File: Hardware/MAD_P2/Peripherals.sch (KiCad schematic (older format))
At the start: 100 parts, among them J12 Micro_SD_Card, U28 DS3231M, U29 ESP-12F

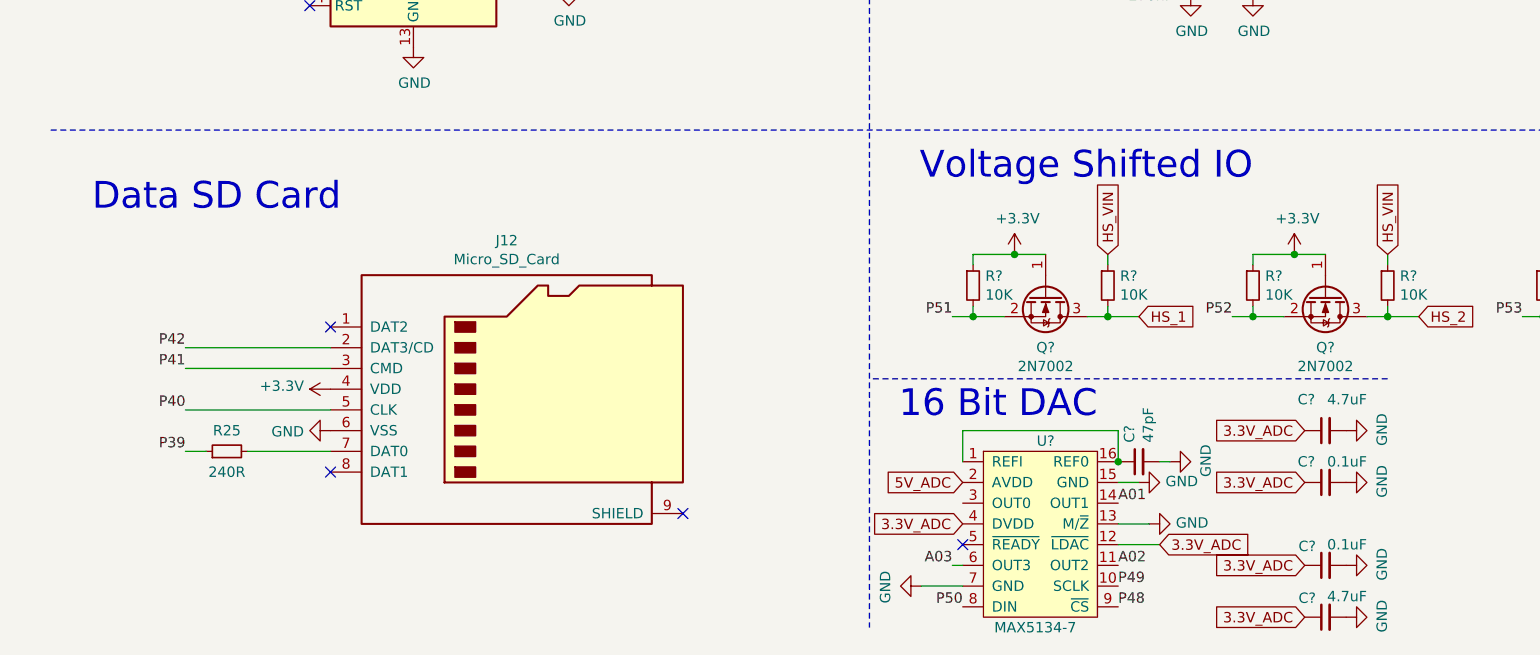
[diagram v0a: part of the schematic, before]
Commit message: added optional sd card socket for data
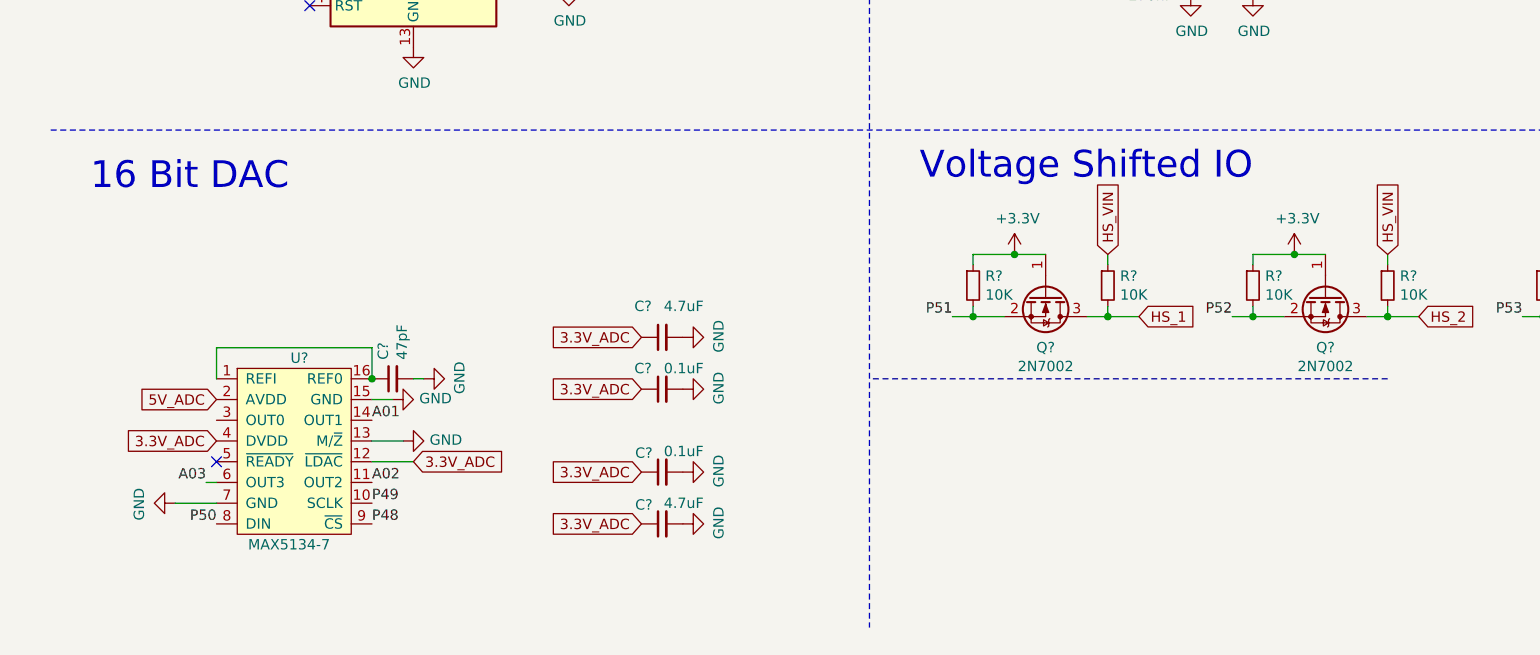
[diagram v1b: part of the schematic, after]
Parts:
- removed J12: Micro_SD_Card, Tensile_Board:WM26501, symbol Connector:Micro_SD_Card
- removed R25: 240R, Resistor_SMD:R_0603_1608Metric, symbol Device:R_Small
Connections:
- no-connect marks 9 -> 6
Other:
- note removed: "Data SD Card"
- moved on the sheet: C?, U?

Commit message: revising pcb layout
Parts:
- C108, C113, C114: renamed from C?; footprint (none) -> Capacitor_SMD:C_0603_1608Metric
- J33: renamed from J?; footprint (none) -> Connector_PinSocket_2.54mm:PinSocket_1x06_P2.54mm_Vertical
- R38, R41, R43, R44, R45, R48, R49, R50, R61: renamed from R?; footprint (none) -> Resistor_SMD:R_0603_1608Metric
- R57, R58, R59, R60, R62, R63, R64, R65: renamed from R?; footprint (none) -> Resistor_SMD:R_0805_2012Metric
- U23: renamed from U?; footprint (none) -> Package_QFP:LQFP-32_5x5mm_P0.5mm
- Y2: renamed from Y?; value Crystal_GND24_Small -> 16.384MHz; footprint (none) -> Crystal:Crystal_SMD_3225-4Pin_3.2x2.5mm
- gave numbers to parts that had none: 47

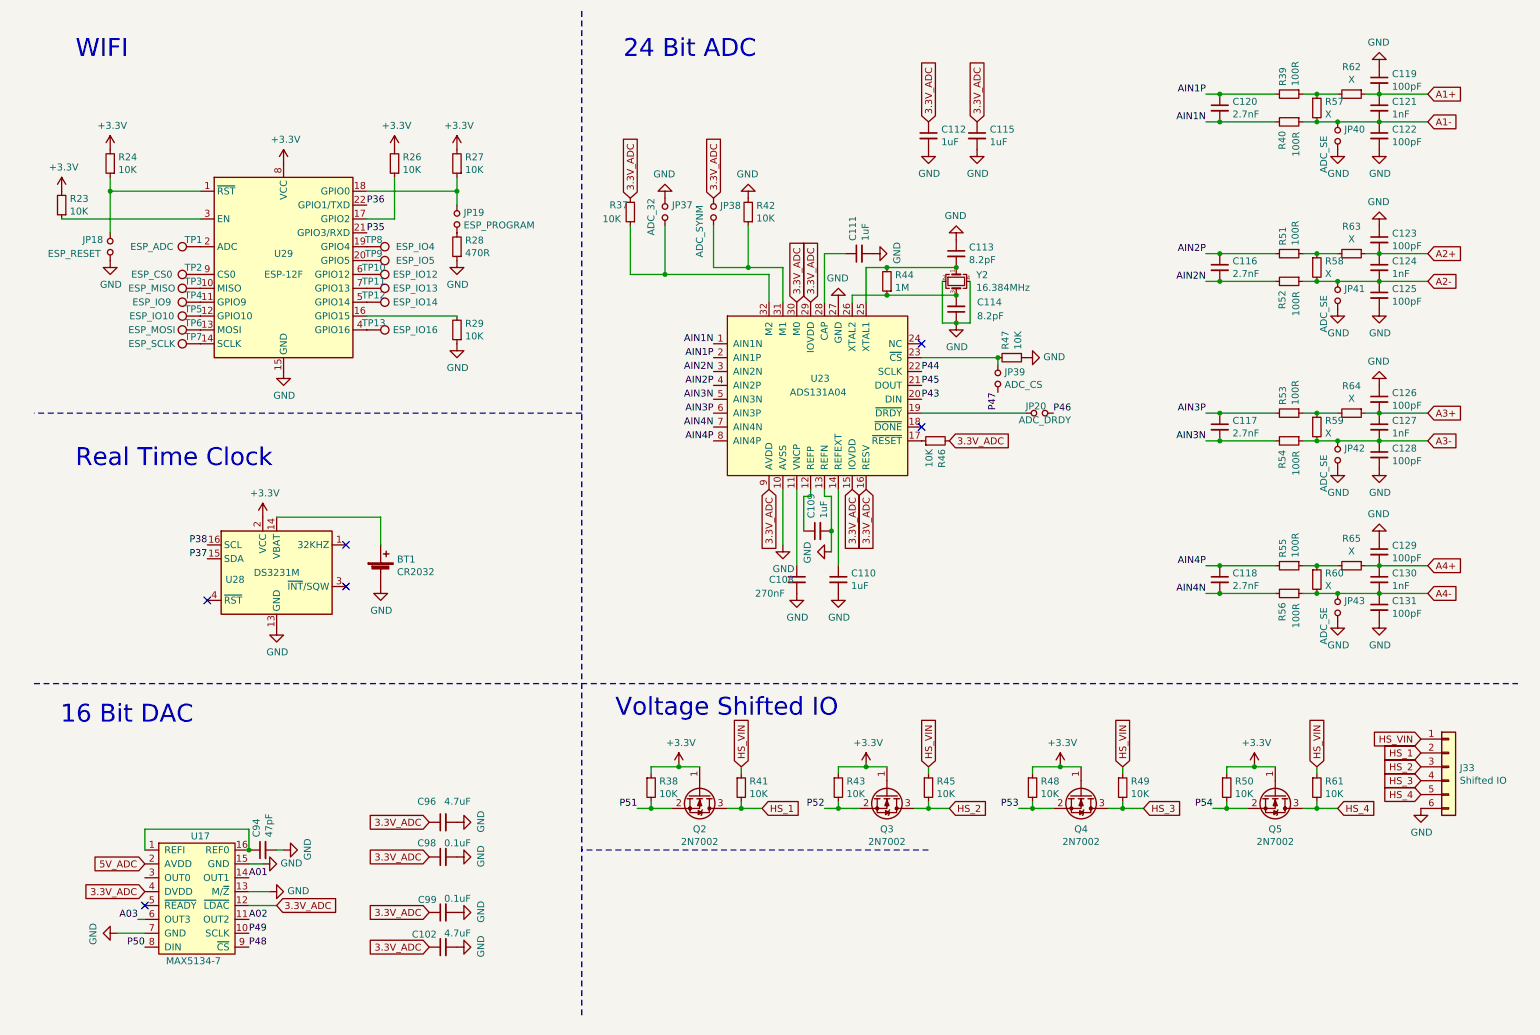
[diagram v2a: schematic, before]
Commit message: routed adc
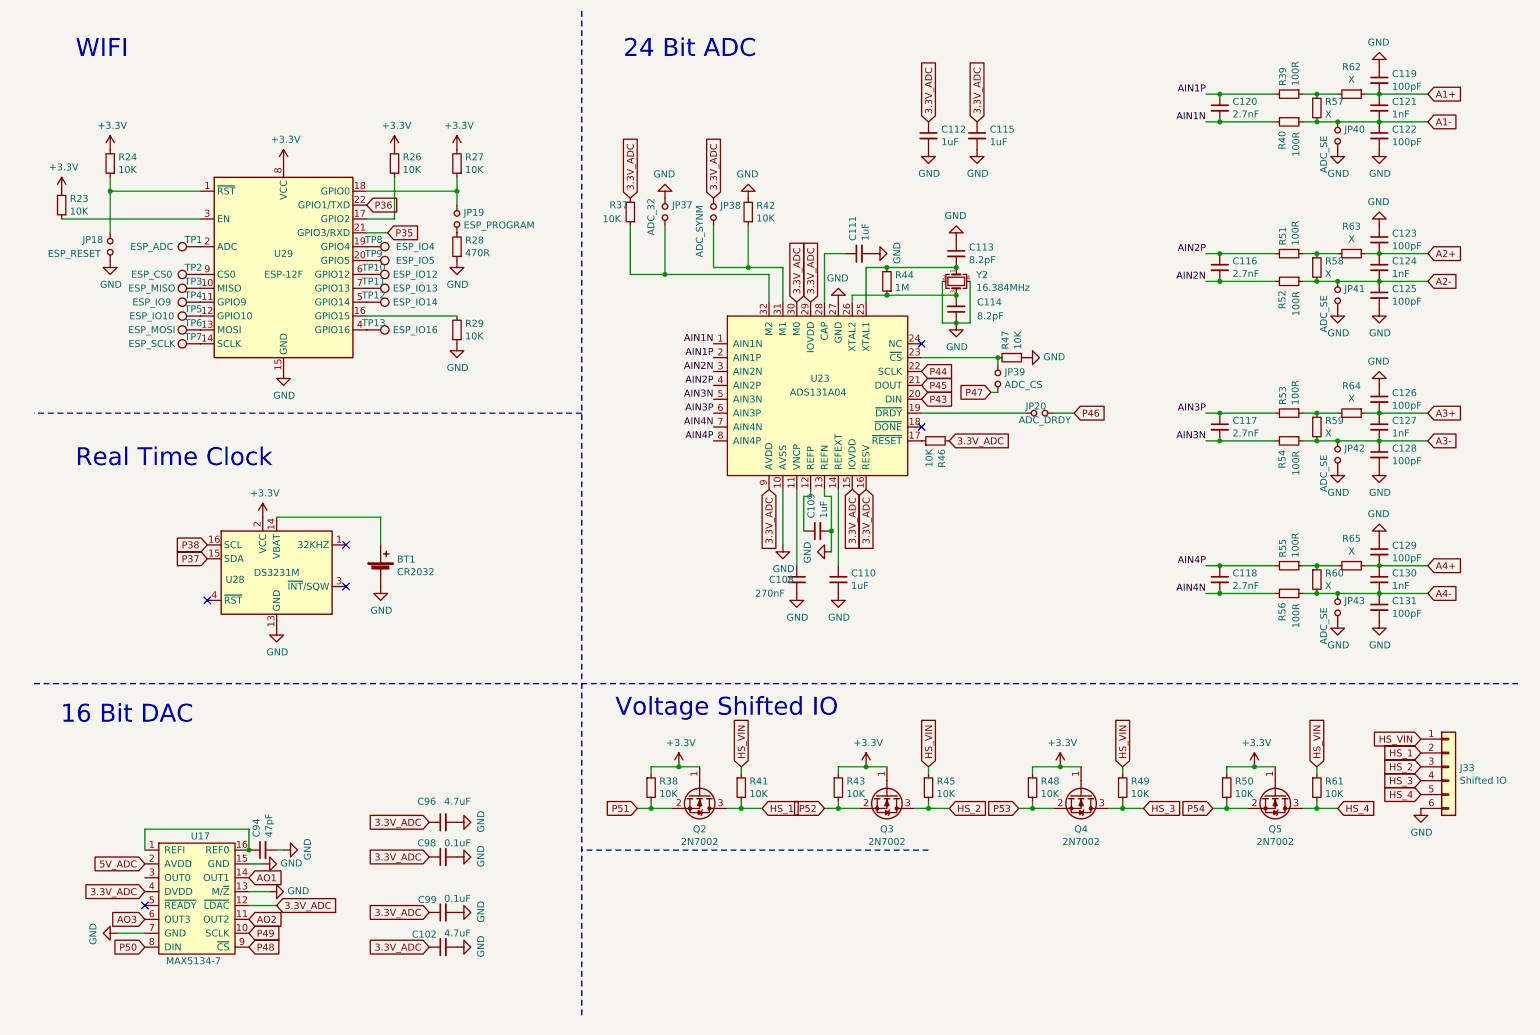
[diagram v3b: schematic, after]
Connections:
- net A01 renamed AO1
- net A02 renamed AO2
- net A03 renamed AO3
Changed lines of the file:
@@
 	0    1    1    0
 $EndComp
-Text Label 2900 2100 0    50   ~ 0
-P35
-Text Label 2900 1900 0    50   ~ 0
-P36
 Text Notes 800  850  0    129  ~ 0
 WIFI
@@
 NoConn ~ 2750 4650
 NoConn ~ 1750 4750
-Text Label 1750 4450 2    50   ~ 0
-P37
-Text Label 1750 4350 2    50   ~ 0
-P38
 NoConn ~ 2750 4350
 $Comp
@@
 Wire Notes Line
 	4450 500  4450 7750
-Text Label 6900 3300 0    50   ~ 0
-P43
-Text Label 6900 3100 0    50   ~ 0
-P44
-Text Label 6900 3200 0    50   ~ 0
-P45
-Text Label 7850 3400 0    50   ~ 0
-P46
 $Comp
 L Device:Jumper_NO_Small JP20
@@
 	0    -1   -1   0
 $EndComp
-Text Label 7450 3250 3    50   ~ 0
-P47
 Wire Wire Line
 	6900 3000 7450 3000
@@
 	0    -1   -1   0
 $EndComp
-Text Label 2050 7250 0    50   ~ 0
-P48
-Text Label 2050 7150 0    50   ~ 0
-P49
-Text Label 1300 7250 2    50   ~ 0
-P50
 $Comp
 L power:GND #PWR0241
@@
 Text GLabel 1300 6650 0    50   Input ~ 0
 5V_ADC
-Text Label 1250 7050 2    50   ~ 0
-A03
-Text Label 2050 7050 0    50   ~ 0
-A02
-Text Label 2050 6750 0    50   ~ 0
-A01
 $Comp
 L power:GND #PWR0243
@@
 	5600 6250 5750 6250
 Connection ~ 5600 6250
-Text Label 4850 6250 2    50   ~ 0
-P51
 Text GLabel 5750 6250 2    50   Input ~ 0
 HS_1
@@
 	6950 6250 7100 6250
 Connection ~ 6950 6250
-Text Label 6200 6250 2    50   ~ 0
-P52
 Text GLabel 7100 6250 2    50   Input ~ 0
 HS_2
@@
 	8350 6250 8500 6250
 Connection ~ 8350 6250
-Text Label 7600 6250 2    50   ~ 0
-P53
 Text GLabel 8500 6250 2    50   Input ~ 0
 HS_3
@@
 	9750 6250 9900 6250
 Connection ~ 9750 6250
-Text Label 9000 6250 2    50   ~ 0
-P54
 Text GLabel 9900 6250 2    50   Input ~ 0
 HS_4
@@
 Wire Wire Line
 	2250 6550 2300 6550
-Wire Wire Line
-	1250 7050 1300 7050
+Text GLabel 2900 1900 2    50   Input ~ 0
+P36
+Text GLabel 3050 2100 2    50   Input ~ 0
+P35
+Wire Wire Line
+	3050 2100 2900 2100
+Text GLabel 6900 3100 2    50   Input ~ 0
+P44
+Text GLabel 6900 3200 2    50   Input ~ 0
+P45
+Text GLabel 6900 3300 2    50   Input ~ 0
+P43
+Text GLabel 7400 3250 0    50   Input ~ 0
+P47
+Wire Wire Line
+	7400 3250 7450 3250
+Text GLabel 8000 3400 2    50   Input ~ 0
+P46
+Wire Wire Line
+	8000 3400 7850 3400
+Text GLabel 1750 4350 0    50   Input ~ 0
+P38
+Text GLabel 1750 4450 0    50   Input ~ 0
+P37
+Text GLabel 1300 7050 0    50   Input ~ 0
+AO3
+Text GLabel 1300 7250 0    50   Input ~ 0
+P50
+Text GLabel 2050 7250 2    50   Input ~ 0
+P48
+Text GLabel 2050 7150 2    50   Input ~ 0
+P49
+Text GLabel 2050 7050 2    50   Input ~ 0
+AO2
+Text GLabel 2050 6750 2    50   Input ~ 0
+AO1
+Text GLabel 4850 6250 0    50   Input ~ 0
+P51
+Text GLabel 6200 6250 0    50   Input ~ 0
+P52
+Text GLabel 7600 6250 0    50   Input ~ 0
+P53
+Text GLabel 9000 6250 0    50   Input ~ 0
+P54
 $EndSCHEMATC

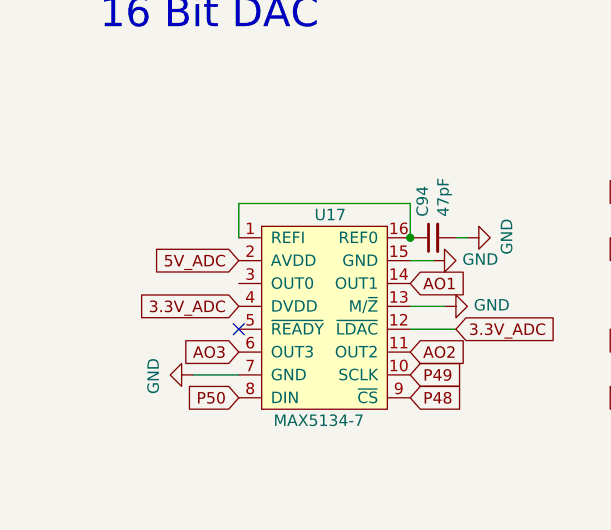
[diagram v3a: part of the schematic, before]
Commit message: fixed DAC issue and added silkscreen
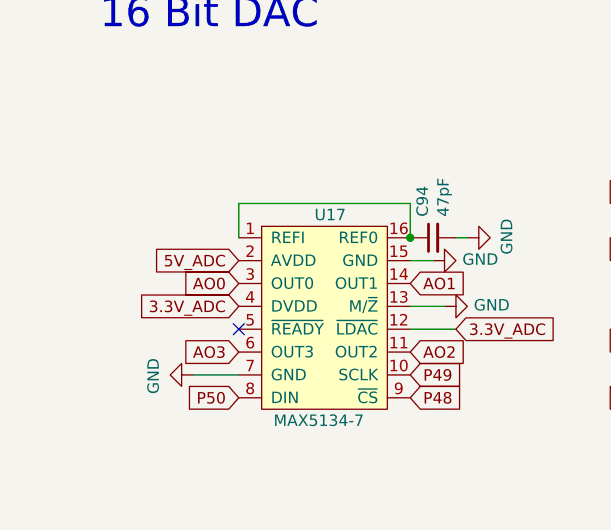
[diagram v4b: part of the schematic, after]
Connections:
- net AO0: now reaches U17.3 (OUT0)
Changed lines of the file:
@@
 Text GLabel 9000 6250 0    50   Input ~ 0
 P54
+Text GLabel 1300 6750 0    50   Input ~ 0
+AO0
 $EndSCHEMATC

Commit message: completed BOM with digikey and LSCS parts
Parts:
- BT1: LCSC (none) -> C70377; TYPE (none) -> EXT
- C102, C96: LCSC (none) -> C19666; TYPE (none) -> BASIC
- C108: LCSC (none) -> C376826; TYPE (none) -> EXT
- C109, C110, C111, C112, C115: LCSC (none) -> C15849; TYPE (none) -> BASIC
- C113, C114: LCSC (none) -> C170126; TYPE (none) -> EXT
- C116, C117, C118, C120: LCSC (none) -> C1609; TYPE (none) -> BASIC
- C119, C122, C123, C125, C126, C128, C129, C131: LCSC (none) -> C14858; TYPE (none) -> BASIC
- C121, C124, C127, C130: LCSC (none) -> C1588; TYPE (none) -> BASIC
- C94: LCSC (none) -> C1671; TYPE (none) -> BASIC
- C98, C99: LCSC (none) -> C14663; TYPE (none) -> BASIC
- J33, JP18, JP19, JP20, JP37, JP38, JP39, JP40, JP41, JP42, JP43, R57, R58, R59, R60, R62, R63, R64, R65, TP1, TP10, TP11, TP12, TP13, TP2, TP3, TP4, TP5, TP6, TP7, TP8, TP9: TYPE (none) -> NA
- Q2, Q3, Q4, Q5: LCSC (none) -> C8545; TYPE (none) -> BASIC
- R23, R24, R26, R27, R29, R37, R38, R41, R42, R43, R45, R46, R47, R48, R49, R50, R61: LCSC (none) -> C25804; TYPE (none) -> BASIC
- R28: LCSC (none) -> C23179; TYPE (none) -> BASIC
- R39, R40, R51, R52, R53, R54, R55, R56: LCSC (none) -> C22775; TYPE (none) -> BASIC
- R44: LCSC (none) -> C22935; TYPE (none) -> BASIC
- U17: DIGIKEY (none) -> MAX5134AGUE; TYPE (none) -> DIGIKEY
- U23: DIGIKEY (none) -> (none); LCSC (none) -> C882747; TYPE (none) -> EXT
- U28: DIGIKEY (none) -> DS3231M; LCSC (none) -> C9866; TYPE (none) -> EXT
- U29: LCSC (none) -> C82891; TYPE (none) -> EXT
- Y2: LCSC (none) -> C13739; TYPE (none) -> EXT

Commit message: added more functionality to JSON for motion quartet, motion set, motion profiles, machine profile, and more
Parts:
- BT1, C108, C113, C114, U17, U23, U28, U29, Y2: ASSEMBLED (none) -> NO
- C102, C109, C110, C111, C112, C115, C116, C117, C118, C119, C120, C121, C122, C123, C124, C125, C126, C127, C128, C129, C130, C131, C94, C96, C98, C99, Q2, Q3, Q4, Q5, R23, R24, R26, R27, R28, R29, R37, R38, R39, R40, R41, R42, R43, R44, R45, R46, R47, R48, R49, R50, R51, R52, R53, R54, R55, R56, R61: ASSEMBLED (none) -> YES
